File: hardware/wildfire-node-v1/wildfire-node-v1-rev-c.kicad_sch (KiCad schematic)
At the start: 30 parts, among them J1 BATT IN (JST-PH 2.0 PROPOSED), Q7 TBD, U1 Heltec HTIT-WB32LAF V4.2, U2 PMS5003, U3 AS3935 (SparkFun SEN-15441), U4 BME680, U5 MiniBoost 5V (TPS61023)

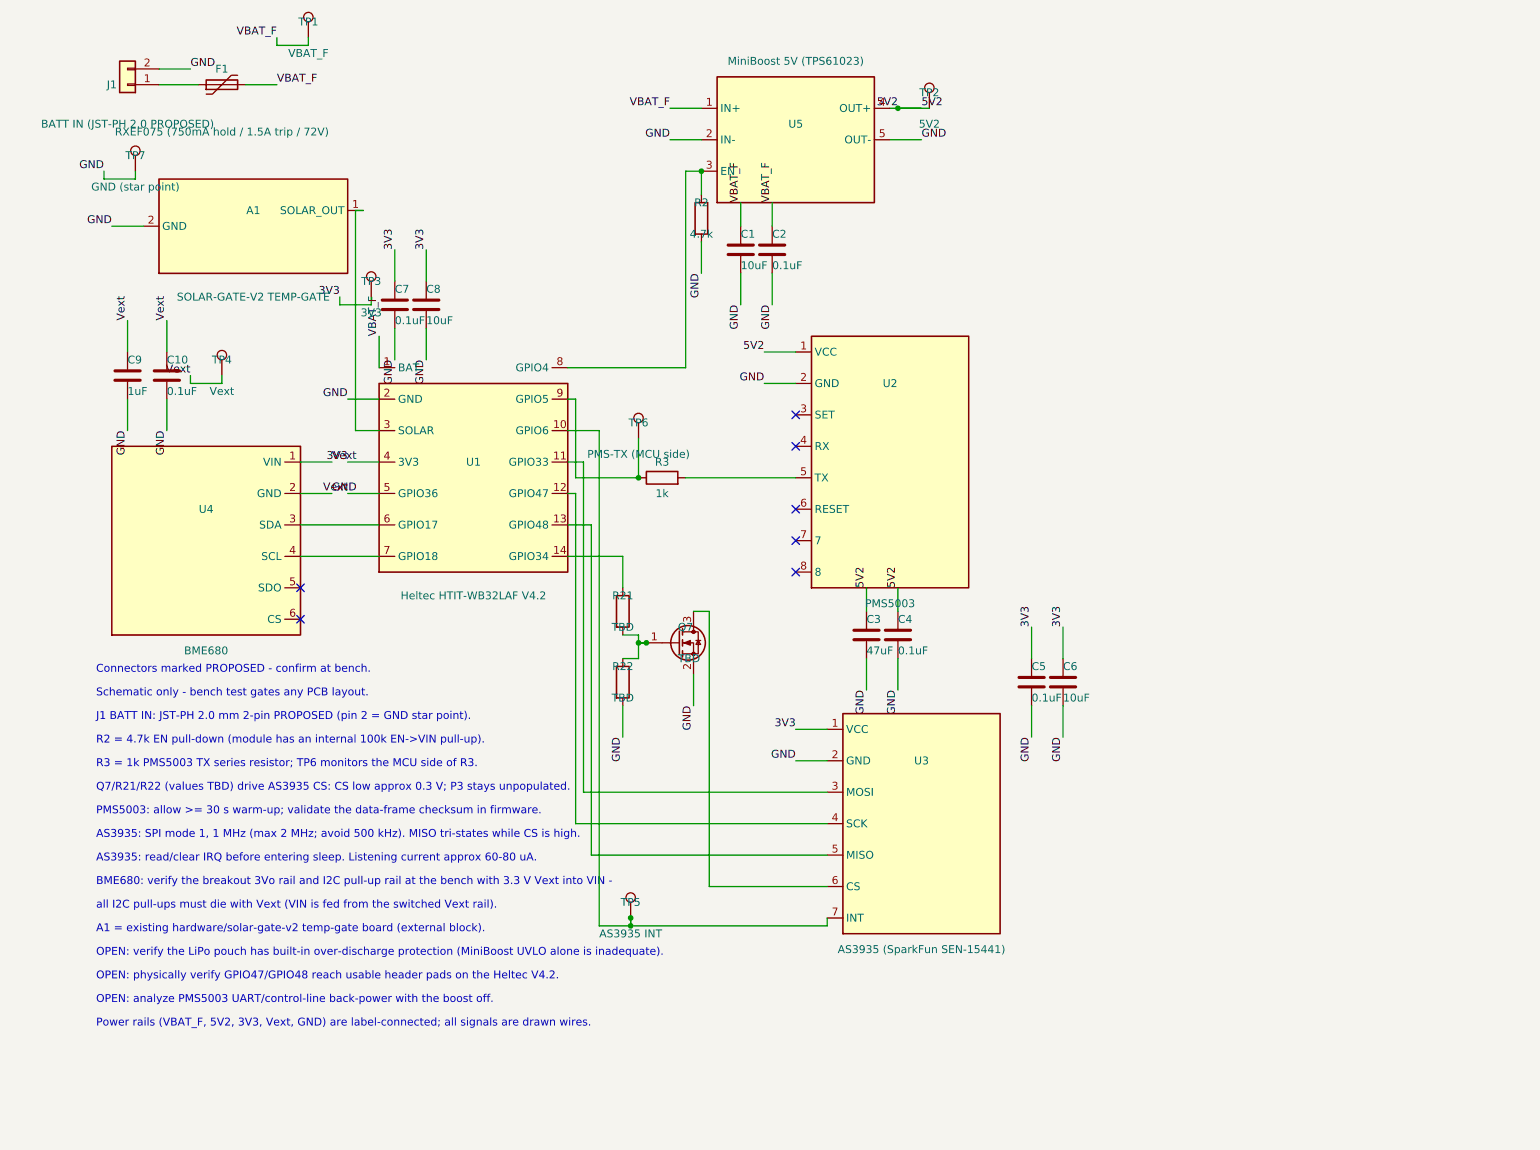
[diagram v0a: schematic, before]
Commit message: 0077: re-lay out the Wildfire Node v1 Rev C schematic for readability
Placement and routing only — the netlist is unchanged (verified against the 0076
revision: 19 multi-pin nets / 77 connected pins, identical partition, identical
members per net, same 7 NC pins; ERC unchanged at 0 errors / 30
[lib_symbol_mismatch] warnings).

Layout: modules now spread across the full sheet width instead of the left ~58 %,
the notes block moved to the bottom-left band with a routing keep-out so no wire
crosses it, all 60 Ref/Value fields were measured in the exported vector and
moved to a free site (0 text-vs-text overlaps, 0 wires crossing a text glyph,
0 wires in the notes/title-block keep-outs), and the three rotated symbols
(J1, F1, R3) get field angles that render their Ref/Value horizontally.

Regenerated .kicad_sch, vector PDF, 600 dpi PNG and the ERC report; README
documents the layout zones and how the sheet was verified.
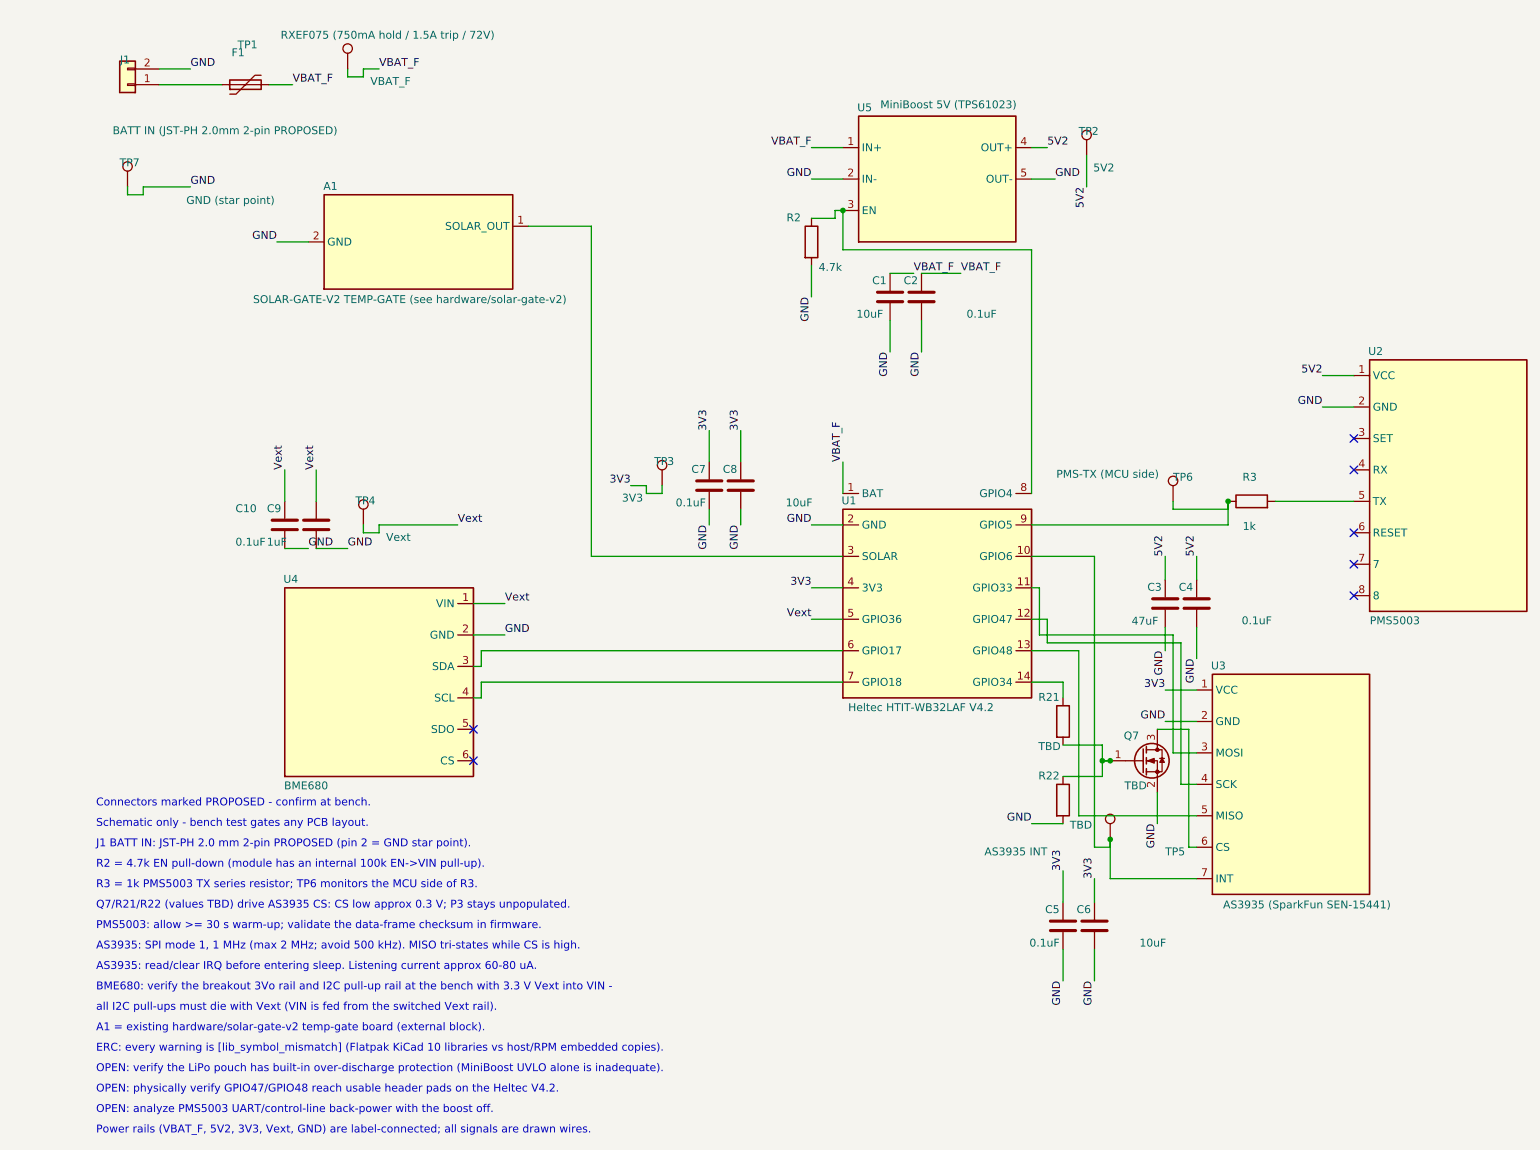
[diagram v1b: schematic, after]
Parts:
- A1: value SOLAR-GATE-V2 TEMP-GATE -> SOLAR-GATE-V2 TEMP-GATE (see hardware/solar-gate-v2)
- J1: value BATT IN (JST-PH 2.0 PROPOSED) -> BATT IN (JST-PH 2.0mm 2-pin PROPOSED)
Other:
- note added: "ERC: every warning is [lib_symbol_mismatch] (Flatpak KiCad 10 libraries vs host/RPM embedded copies)."
